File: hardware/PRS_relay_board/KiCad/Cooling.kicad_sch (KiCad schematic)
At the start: 15 parts

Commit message: Commit
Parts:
- C19: renamed from C?; value (none) -> 100n; footprint (none) -> Capacitor_SMD:C_0603_1608Metric_Pad1.08x0.95mm_HandSolder
- D9: renamed from D?; value (none) -> MMBD7000HC; footprint (none) -> Package_TO_SOT_SMD:SOT-23_Handsoldering
- J6: renamed from J?; value (none) -> B3B-XH-A; footprint (none) -> Connector_JST:JST_XH_B3B-XH-A_1x03_P2.50mm_Vertical
- Q5: renamed from Q?; value (none) -> BC848; footprint (none) -> Package_TO_SOT_SMD:SOT-23_Handsoldering
- Q6: renamed from Q?; value (none) -> PMV37ENEA; footprint (none) -> Package_TO_SOT_SMD:SOT-23_Handsoldering
- R37, R38, R39, R40, R44, R9: renamed from R?; value (none) -> 10k; footprint (none) -> Resistor_SMD:R_0603_1608Metric_Pad0.98x0.95mm_HandSolder
- R41: renamed from R?; value (none) -> -; footprint (none) -> Resistor_SMD:R_0603_1608Metric_Pad0.98x0.95mm_HandSolder; Comment (none) -> DNP
- R42, R43: renamed from R?; value (none) -> R; footprint (none) -> Resistor_SMD:R_0603_1608Metric_Pad0.98x0.95mm_HandSolder
- U1: renamed from IC?; value (none) -> STCN75; footprint (none) -> STCN75:SOP65P490X110-8N

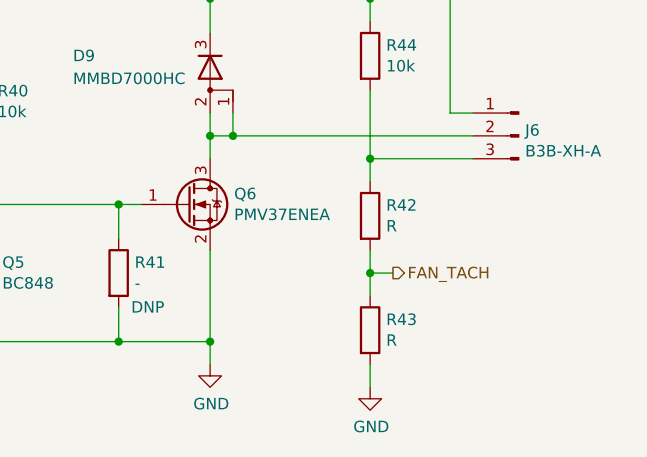
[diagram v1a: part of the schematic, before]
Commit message: Set fan resistor values
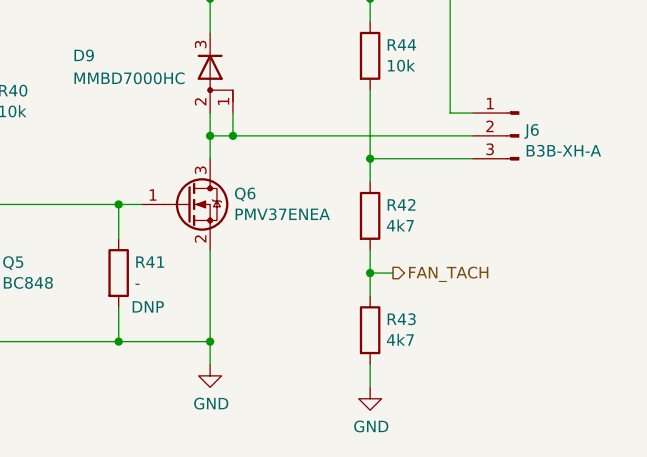
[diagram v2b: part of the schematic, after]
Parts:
- R42, R43: value R -> 4k7
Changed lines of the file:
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@@
   (title_block
     (title "PRS Cooling")
-    (date "2021-10-12")
+    (date "2023-02-20")
     (rev "1.0")
     (company "Deeply Embedded OÜ")
@@
       (effects (font (size 1.27 1.27)) (justify left))
     )
-    (property "Value" "R" (id 1) (at 231.648 78.613 0)
+    (property "Value" "4k7" (id 1) (at 231.648 78.613 0)
       (effects (font (size 1.27 1.27)) (justify left))
     )
@@
       (effects (font (size 1.27 1.27)) hide)
     )
+    (property "Description" "RES 4k7 5% 100mW 0603" (id 4) (at 229.87 77.47 0)
+      (effects (font (size 1.27 1.27)) hide)
+    )
     (pin "1")
     (pin "2")
@@
       (effects (font (size 1.27 1.27)) (justify left))
     )
-    (property "Value" "R" (id 1) (at 231.648 91.313 0)
+    (property "Value" "4k7" (id 1) (at 231.648 91.313 0)
       (effects (font (size 1.27 1.27)) (justify left))
     )
@@
       (effects (font (size 1.27 1.27)) hide)
     )
+    (property "Description" "RES 4k7 5% 100mW 0603" (id 4) (at 229.87 90.17 0)
+      (effects (font (size 1.27 1.27)) hide)
+    )
